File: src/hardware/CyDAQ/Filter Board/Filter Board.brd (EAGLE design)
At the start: 160.9 x 110.9 mm, 218 parts, among them J1 DCJ0202, J10 Vout_HEADER, J11 5V0_SENSOR, J12 3V3_SENSOR, J13 1V8_SENSOR, J14 BRKOUT_JD, J15 BRKOUT_JC, J16 BRKOUT_JB, J17 BRKOUT_JF, J18 5V0_CONN, J19 3V3_CONN, J2 ZYBO_JF, J20 1V8_CONN, J3 ZYBO_JE, J4 ZYBO_JD, J5 ZYBO_JC, J6 ZYBO_JB, J7 A_XADC, J8 SJ1-3523N, J9 Vin_HEADER, U1 TPS54531DDARDDA8_3P1X2P4-L, U10 CD74HCT4051, U11 CD74HCT4051, U12 OPA4197, U13 OPA4197, U14 OPA4197, U15 OPA4197, U16 OPA4197, U17 CD74HCT4053, U18 CD74HCT4051, U19 OPA2197, U2 VS-50WQ04FNPBFDPAK-L, U3 TPS56339, U4 TPS56339, U5 LM43601PWPR, U6 X9258_A, U7 X925_B, U8 X9258_C, U9 X9258_D

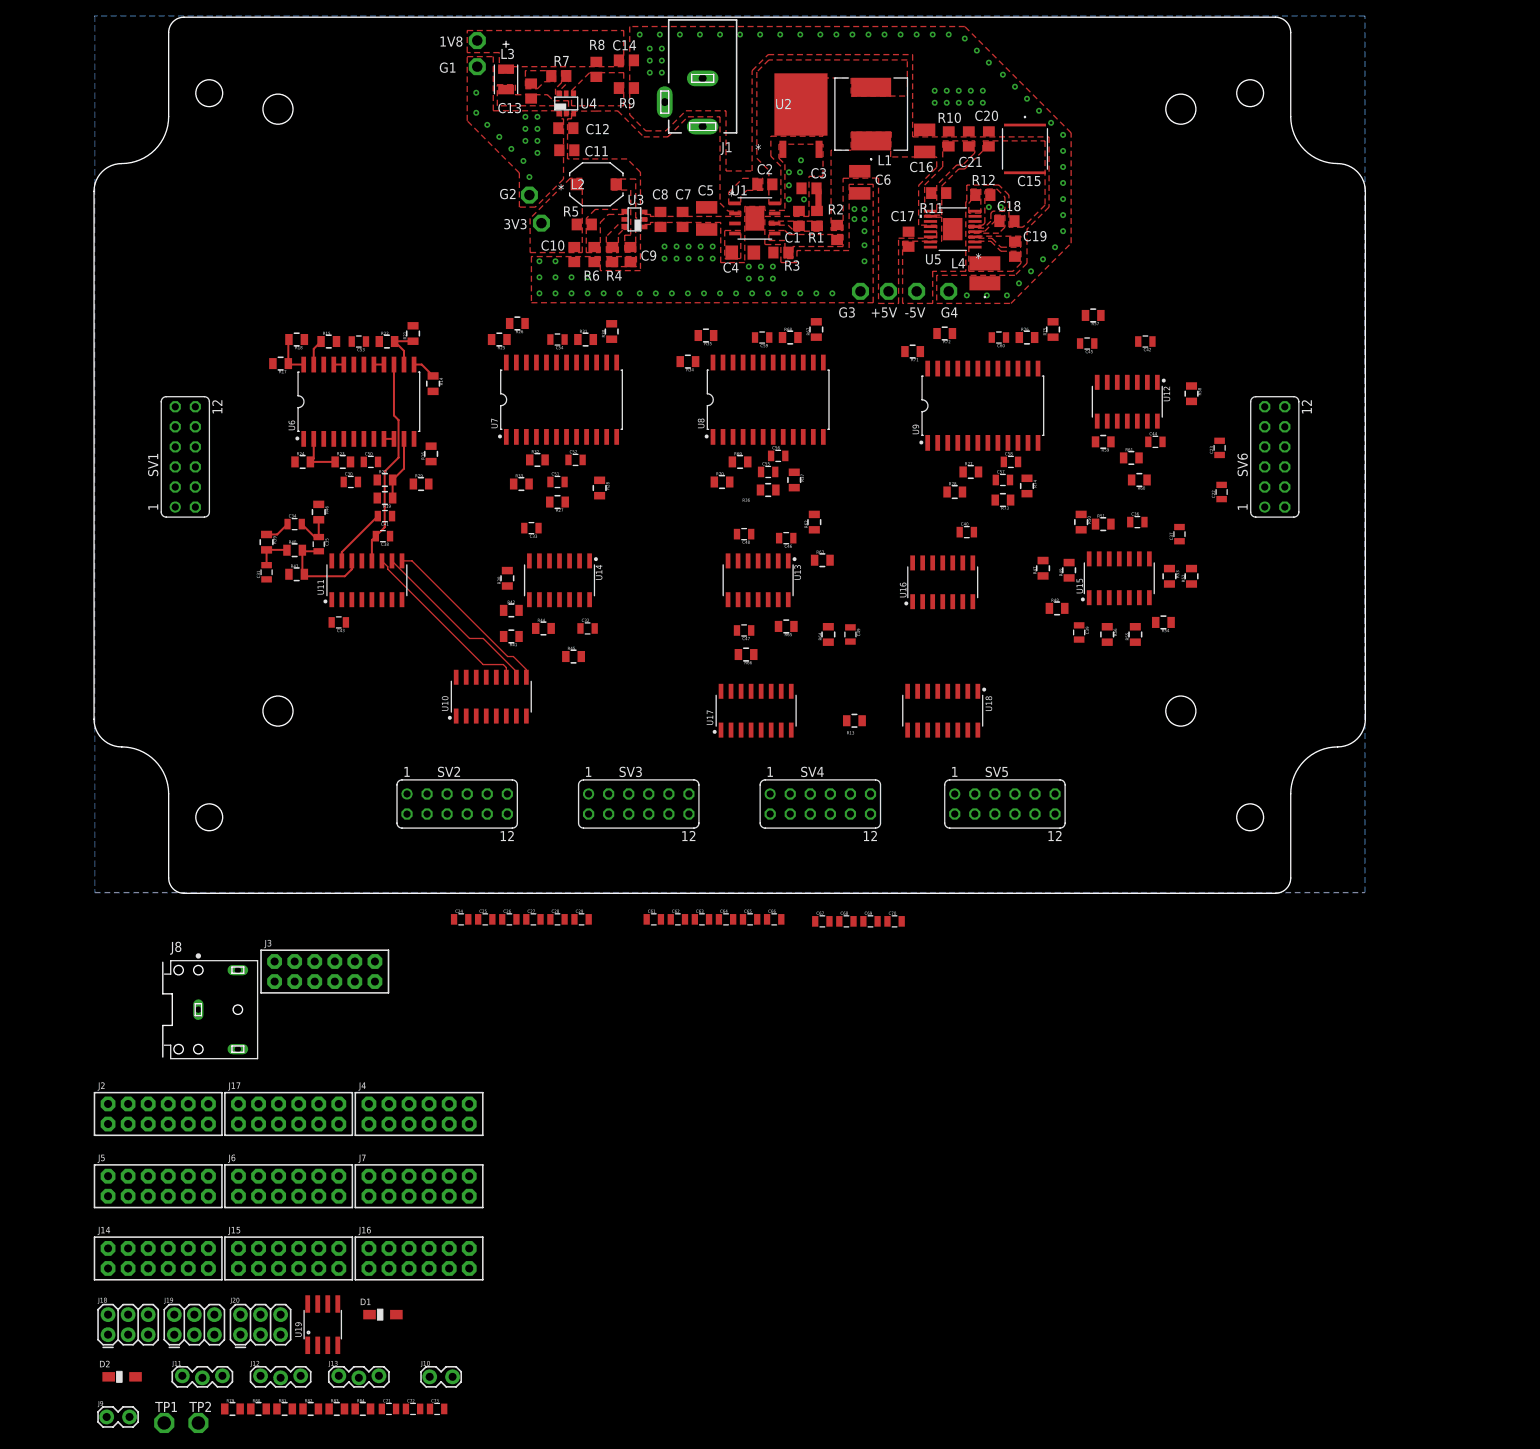
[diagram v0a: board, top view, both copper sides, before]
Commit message: Placed components and started routing
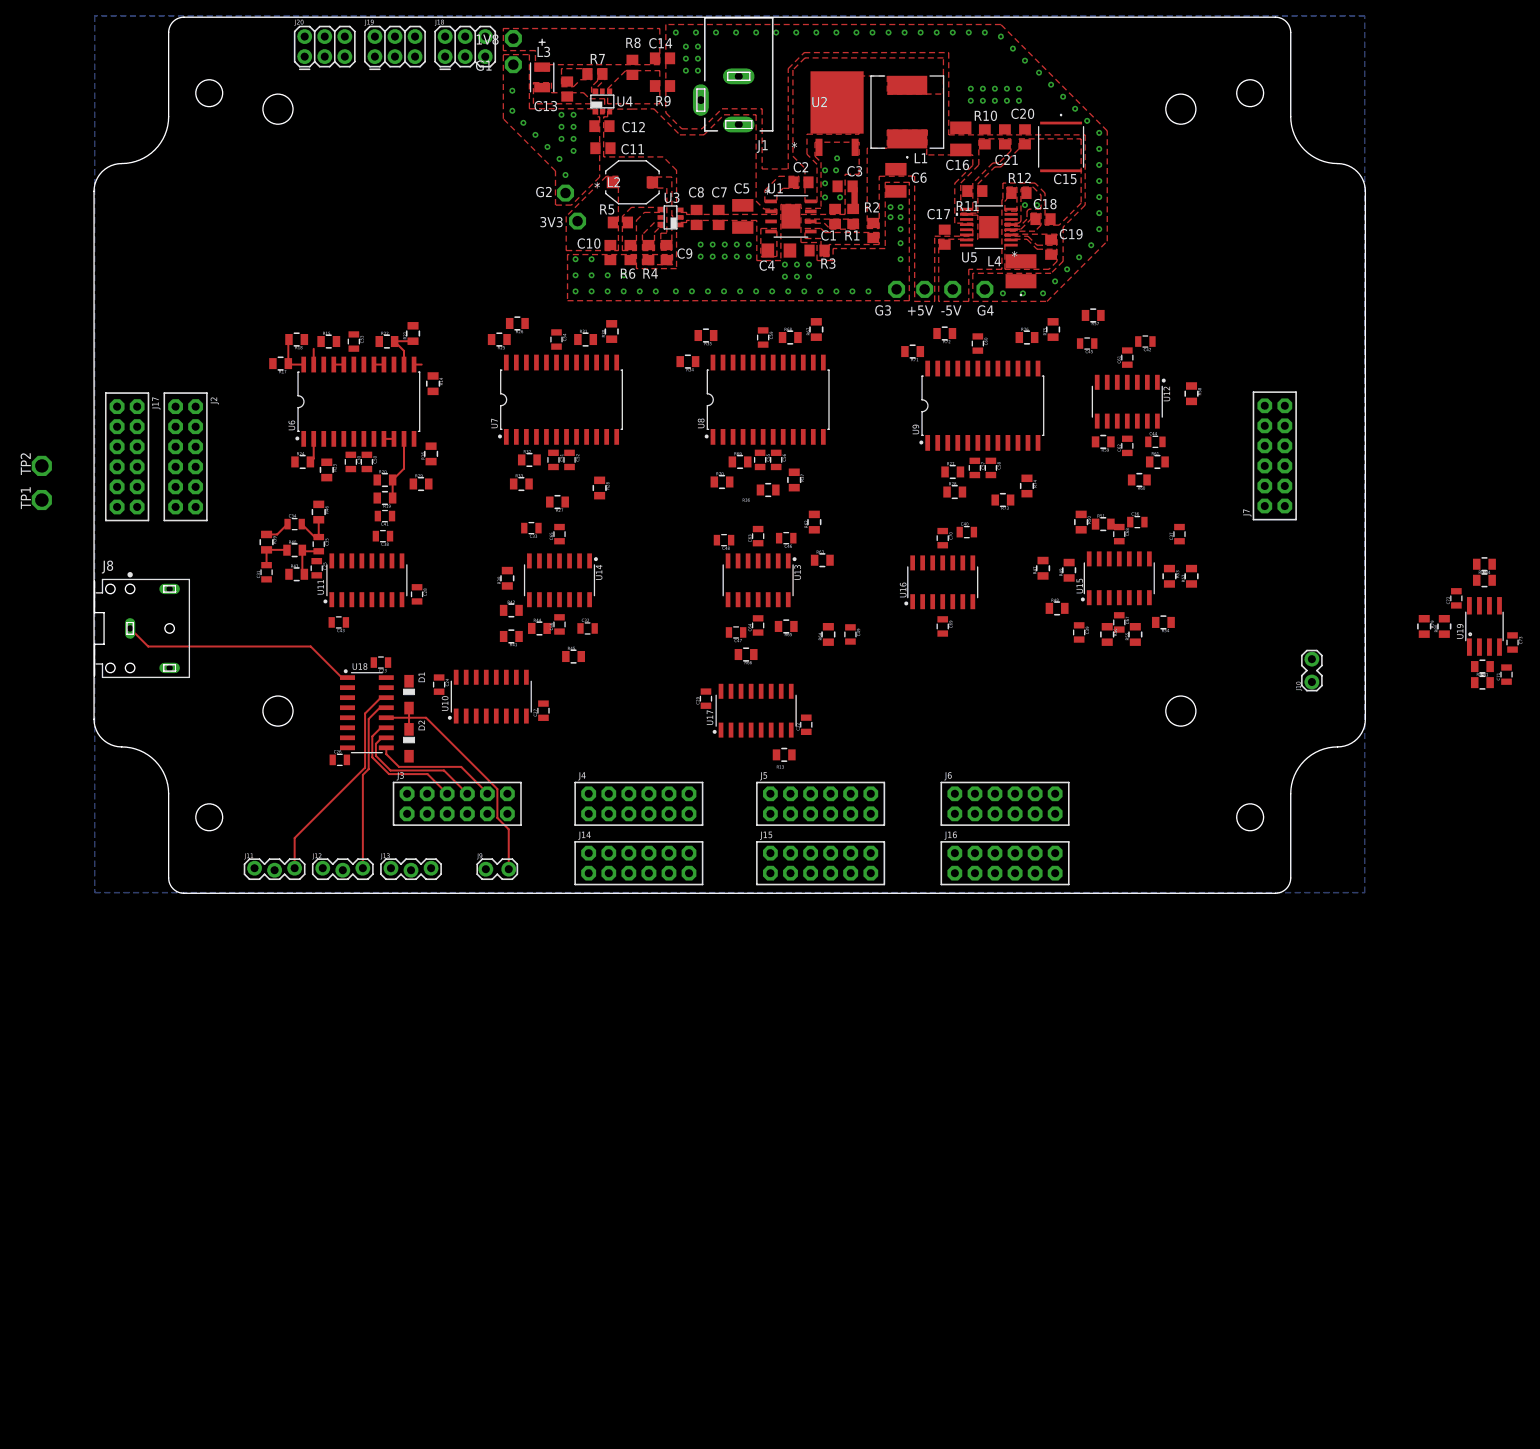
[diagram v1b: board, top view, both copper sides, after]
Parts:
- removed SV1, SV2, SV3, SV4, SV5, SV6: (no value), con-lsta:FE06-2
- moved R79 180.5 mm to (168.4, 33.8), turned to 270 degrees
- moved R80 179.9 mm to (170.9, 33.8), turned to 90 degrees
- moved R83 179.2 mm to (176.0, 39.6)
- moved R81 178.4 mm to (175.8, 28.7), turned to 180 degrees
- moved R84 177.7 mm to (176.0, 41.7), turned to 180 degrees
- moved R82 174.5 mm to (175.8, 26.7)
- moved U19 171.6 mm to (176.0, 33.8)
- moved C71 169.3 mm to (178.8, 27.7), turned to 90 degrees
- moved J18 167.3 mm to (44.5, 105.9)
- moved C72 167.3 mm to (172.5, 37.3), turned to 90 degrees
- moved C73 167.2 mm to (179.6, 31.8), turned to 270 degrees
- moved J19 163.8 mm to (35.6, 105.9)
- moved J20 162.0 mm to (26.7, 105.9)
- moved J7 145.2 mm to (150.7, 49.0), turned to 90 degrees
- moved J10 142.1 mm to (154.2, 26.9), turned to 90 degrees
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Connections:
- removed net N$60: C44.2, J7.3, J7.4, R61.2, U12.14, U9.16, U9.17
- net 1V8SENSOR_IN: now also U18.13; no longer U18.15
- net 3V3SENSOR_IN: now also U18.14; no longer U18.13
- net 5V0SENSOR_IN: now also U18.15; no longer U18.14
- net GND: now also C44.2, J7.3, J7.4, R61.2, U12.14, U9.16, U9.17
- net SCL: now also R14.1; no longer R15.1
- net SDA: now also R15.1; no longer R14.1
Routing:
- net ANALOGUE_IN: track 0.00 -> 31.2 mm
- net 3.5MM_IN: track 0.00 -> 30.1 mm
- net LP1_OUT: track 26.5 -> 0.00 mm
- net 5V0SENSOR_IN: track 0.00 -> 26.1 mm
- net FILT_SELECT0: track 22.7 -> 0.00 mm
- net FILT_SELECT2: track 22.4 -> 0.00 mm
- net FILT_SELECT1: track 22.7 -> 0.47 mm
- net 3V3SENSOR_IN: track 0.00 -> 21.2 mm
- net INPUT_SELECT1: track 0.00 -> 16.7 mm
- net INPUT_SELECT0: track 0.00 -> 16.3 mm
- net INPUT_SELECT2: track 0.00 -> 15.7 mm
- net HP1_OUT: track 8.83 -> 1.27 mm
- net NOTCH_OUT: track 12.8 -> 5.28 mm
- net N$44: track 6.22 -> 3.09 mm
- net SDA: track 3.01 -> 0.97 mm
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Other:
- outline, holes or cut-outs redrawn

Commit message: Continued routing.
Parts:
- moved C40 69.6 mm to (46.2, 19.1), turned to 180 degrees
- moved C70 63.4 mm to (49.3, 19.8), turned to 90 degrees
- moved U16 59.8 mm to (49.3, 25.4), turned to 270 degrees
- moved C69 58.2 mm to (49.3, 31.0), turned to 90 degrees
- moved C24 29.9 mm to (73.2, 21.1), turned to 90 degrees
- moved U10 16.4 mm to (66.5, 22.6), turned to 270 degrees
- moved C27 3.30 mm to (59.9, 24.4), turned to 270 degrees
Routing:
- net 1V8SENSOR_IN: track 0.00 -> 25.9 mm
- net ANALOGUE_IN: track 31.2 -> 39.2 mm
- net 3V3SENSOR_IN: track 21.2 -> 23.8 mm
- net 5V0SENSOR_IN: track 26.1 -> 28.4 mm

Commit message: Finished routing BP filter
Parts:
- added R85: 10k, Resistors:0805
- moved C43 196.6 mm to (217.7, 96.0), turned to 270 degrees
- moved U11 187.6 mm to (212.3, 99.6), turned to 180 degrees
- moved C28 186.1 mm to (214.1, 105.9), turned to 0 degrees
- moved C24 184.0 mm to (229.6, 117.9)
- moved C27 184.0 mm to (216.4, 121.2)
- moved U10 184.0 mm to (223.0, 119.4)
- moved R32 167.8 mm to (221.7, 74.9), turned to 270 degrees
- moved R33 166.7 mm to (219.2, 74.9), turned to 90 degrees
- moved R27 165.2 mm to (219.2, 88.6), turned to 90 degrees
- moved R66 163.9 mm to (228.9, 104.1), turned to 0 degrees
- moved C51 163.6 mm to (219.7, 80.8), turned to 0 degrees
- moved C46 163.5 mm to (240.0, 104.1), turned to 0 degrees
- moved C52 161.9 mm to (219.7, 82.8), turned to 0 degrees
- moved R28 161.8 mm to (221.5, 88.6)
- moved C33 159.9 mm to (214.9, 57.7), turned to 0 degrees
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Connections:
- new net BP6_HPOUT: C44.2, R61.2, U12.8, U9.16, U9.17
- net !SYSTEM_EN: now also R85.1
- net BP6_OUT: now also U13.6, U13.7; no longer U14.1, U14.2
- net GND: now also R85.2, U12.10, U13.12, U14.10; no longer C44.2, R61.2, U12.14, U12.5, U13.5, U14.5, U9.16, U9.17
- net HP2_OUT1: now also U14.1; no longer U14.8
- net INPUT_SELECT0: now also J3.10; no longer J3.6
- net INPUT_SELECT2: now also J3.6; no longer J3.10
- net LP2_OUT1: now also U14.14; no longer U14.7
- net N$22: now also U14.5; no longer U12.3
- net N$23: now also U14.6, U14.7; no longer U12.1, U12.2
- net N$24: now also U12.2; no longer U12.9
- net N$25: now also U14.3; no longer U14.10
- net N$26: now also U14.2; no longer U14.9
- net N$28: now also U14.9; no longer U14.13
- net N$29: now also U14.8; no longer U14.14
- net N$30: now also U14.13; no longer U14.6
- net N$57: now also U12.3; no longer U12.10
- net N$58: now also U12.1, U9.20, U9.21; no longer U12.8, U9.10, U9.9
- net N$59: now also U12.9, U9.22; no longer U12.13, U9.8
- net N$61: now also U12.13; no longer U12.6
- net N$62: now also U12.14, U9.10, U9.9; no longer U12.7, U9.20, U9.21
- net N$63: now also U12.5, U9.8; no longer U13.3, U9.22
- net N$64: now also U12.6, U12.7; no longer U13.1, U13.2
- net N$65: now also U13.2; no longer U13.13
- net N$66: now also U13.3; no longer U13.12
- net N$67: now also U13.1; no longer U13.14
- net N$68: now also U13.13; no longer U13.9
- net N$69: now also U13.14; no longer U13.8
- net N$70: now also U13.9; no longer U13.6
- net N$71: now also U13.8; no longer U13.7
- net N$72: now also U13.5; no longer U14.3
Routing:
- net N$67: track 0.00 -> 42.3 mm
- net N$62: track 0.00 -> 39.0 mm
- net N$69: track 0.00 -> 36.1 mm
- net BP6_HPOUT: track 0.00 -> 31.6 mm
- net N$72: track 0.00 -> 31.1 mm
- net N$63: track 0.00 -> 29.9 mm
- net N$58: track 0.00 -> 27.9 mm
- net N$61: track 0.00 -> 22.7 mm
- net N$71: track 0.00 -> 22.7 mm
- net N$68: track 0.00 -> 20.0 mm
- net N$70: track 0.00 -> 17.6 mm
- net N$24: track 0.00 -> 12.8 mm
- net N$59: track 0.00 -> 12.3 mm
- net N$65: track 0.00 -> 9.87 mm
- net -5V0: track 0.00 -> 9.74 mm
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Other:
- board text added: "1st & 2nd Order Filters"
- board text added: "Notch Filter"

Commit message: Rearranged some components for clarity
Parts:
- moved C31 295.4 mm to (242.8, 139.2)
- moved R39 295.4 mm to (242.8, 143.0)
- moved C25 295.4 mm to (249.2, 139.7)
- moved C34 295.4 mm to (246.4, 145.3)
- moved C35 295.4 mm to (249.4, 142.7)
- moved R40 295.4 mm to (246.4, 142.0)
- moved R43 295.4 mm to (246.6, 138.9)
- moved R46 295.4 mm to (249.4, 146.8)
- moved R18 265.3 mm to (229.9, 128.5), turned to 90 degrees
- moved R17 265.0 mm to (226.8, 130.6), turned to 90 degrees
- moved R15 260.5 mm to (229.6, 124.5), turned to 270 degrees
- moved C53 256.9 mm to (229.6, 121.3), turned to 180 degrees
- moved R22 252.3 mm to (229.6, 117.1), turned to 270 degrees
- moved R24 251.8 mm to (214.4, 127.8), turned to 270 degrees
- moved U6 249.7 mm to (222.0, 120.7), turned to 0 degrees
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
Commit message: Continued routing ~ 80% done
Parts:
- moved R15 230.0 mm to (6.60, 68.1)
- moved R14 219.7 mm to (8.89, 67.8), turned to 270 degrees
- moved R16 205.9 mm to (14.2, 67.8), turned to 90 degrees
- moved R29 205.1 mm to (11.4, 67.8)
- moved C70 177.9 mm to (226.1, 39.6), turned to 180 degrees
- moved U16 171.3 mm to (220.0, 39.6), turned to 0 degrees
- moved C40 169.0 mm to (214.4, 36.1), turned to 270 degrees
- moved C69 164.8 mm to (213.9, 39.6), turned to 180 degrees
- moved C22 142.7 mm to (227.6, 59.9), turned to 270 degrees
- moved U17 142.3 mm to (220.5, 62.7), turned to 270 degrees
- moved C29 141.9 mm to (213.4, 65.5), turned to 270 degrees
- moved R13 141.0 mm to (218.6, 69.1), turned to 270 degrees
- moved R36 126.7 mm to (210.1, 28.4), turned to 0 degrees
- moved R68 123.6 mm to (210.1, 49.8), turned to 180 degrees
- moved R37 123.2 mm to (210.1, 31.2), turned to 180 degrees
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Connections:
- net FILTER_IN: now also U16.10; no longer U16.12
- net FILTER_OUT_BUFF: now also U16.13, U16.14; no longer U16.6, U16.7
- net GND: now also U15.5, U16.5, U6.15, U7.5; no longer U15.10, U16.10, U6.22, U7.15
- net HP2_OUT2: now also U15.8, U8.3, U8.4; no longer U15.1, U8.20, U8.21
- net HP2_OUT3: now also U15.1; no longer U15.7
- net LP1_IN: now also U6.20, U6.21; no longer U6.16, U6.17
- net LP1_OUT: now also U6.22; no longer U6.15
- net LP2_OUT1: now also U14.8; no longer U14.14
- net LP2_OUT2: now also U15.7; no longer U15.14
- net LP2_OUT3: now also U16.7; no longer U16.8
- net N$22: now also U6.16, U6.17; no longer U6.20, U6.21
- net N$28: now also U14.13; no longer U14.9
- net N$29: now also U14.14, U7.16, U7.17; no longer U14.8, U7.3, U7.4
- net N$30: now also U14.9, U7.15; no longer U14.13, U7.5
- net N$31: now also U15.10; no longer U15.3
- net N$32: now also U15.9; no longer U15.2
- net N$34: now also U15.13, U8.5; no longer U15.9, U8.22
- net N$35: now also U15.14, U8.20, U8.21; no longer U15.8, U8.3, U8.4
- net N$36: now also U15.6, U8.22; no longer U15.13, U8.5
- net N$37: now also U15.3; no longer U15.5
- net N$38: now also U15.2; no longer U15.6
- net N$42: now also U16.6; no longer U16.9
- net N$43: now also U16.12; no longer U16.5
- net N$72: now also U7.3, U7.4; no longer U7.16, U7.17
- net VIN_BUFFERED: now also U16.8, U16.9; no longer U16.13, U16.14
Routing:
- net HP2_OUT2: track 0.00 -> 57.1 mm
- net N$41: track 0.00 -> 55.1 mm, vias 0 -> 2
- net LP2_OUT3: track 0.00 -> 50.0 mm, vias 0 -> 2
- net LP2_OUT2: track 0.00 -> 48.8 mm
- net HP2_OUT3: track 0.00 -> 48.8 mm, vias 0 -> 2
- net N$22: track 0.00 -> 39.2 mm
- net N$36: track 0.00 -> 32.5 mm
- net HP1_OUT: track 0.00 -> 30.5 mm
- net N$35: track 0.00 -> 29.2 mm
- net HP/LP2_IN2: track 0.00 -> 28.8 mm
- net N$34: track 0.00 -> 28.8 mm
- net HP2_OUT1: track 1.27 -> 28.2 mm
- net HP/LP2_IN3: track 0.00 -> 24.3 mm
- net N$28: track 0.00 -> 22.0 mm
- net N$43: track 0.00 -> 21.4 mm
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- added copper zone on layer 2, net GND
- removed copper zone on layer 16, net GND
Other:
- board text removed: "1st & 2nd Order Filters"

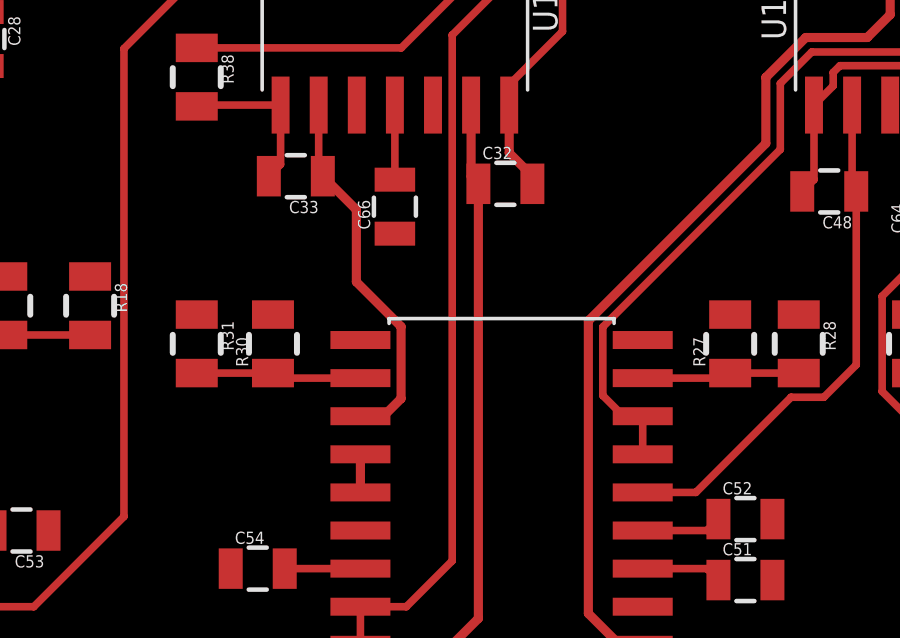
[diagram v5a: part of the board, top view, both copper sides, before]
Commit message: Added some more traces!
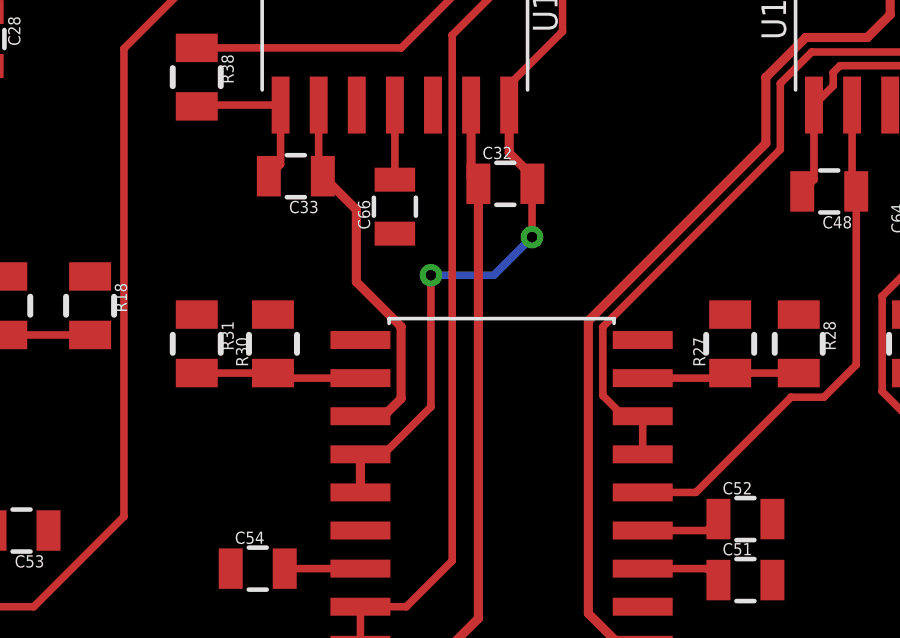
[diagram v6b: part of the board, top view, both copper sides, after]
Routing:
- net N$29: track 21.9 -> 35.0 mm, vias 0 -> 2

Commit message: Used Gateswap magic to clean up some routing
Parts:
- moved R38 16.5 mm to (268.2, 55.1), turned to 0 degrees
- moved C32 7.38 mm to (261.2, 37.8), turned to 180 degrees
- moved C33 7.15 mm to (268.7, 37.8), turned to 0 degrees
- moved R45 2.40 mm to (263.9, 52.3), turned to 180 degrees
- moved R41 2.29 mm to (268.2, 52.3)
- moved R44 1.55 mm to (263.9, 55.1), turned to 0 degrees
- moved R42 1.02 mm to (268.2, 49.0)
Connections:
- net HP2_OUT1: now also U7.16, U7.17; no longer U7.20, U7.21
- net LP2_OUT1: now also U14.14; no longer U14.8
- net N$28: now also U14.9, U7.15; no longer U14.13, U7.22
- net N$29: now also U14.8, U7.20, U7.21; no longer U14.14, U7.16, U7.17
- net N$30: now also U14.13, U7.22; no longer U14.9, U7.15
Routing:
- net N$30: track 12.5 -> 21.8 mm
- net N$28: track 22.0 -> 12.8 mm
- net N$26: track 15.0 -> 7.20 mm
- net HP2_OUT1: track 28.2 -> 24.7 mm
- net N$22: track 39.2 -> 35.9 mm
- net N$29: track 35.0 -> 38.2 mm, vias 2 -> 0
- net LP2_OUT1: track 5.35 -> 3.51 mm
- net N$25: track 9.12 -> 9.77 mm
